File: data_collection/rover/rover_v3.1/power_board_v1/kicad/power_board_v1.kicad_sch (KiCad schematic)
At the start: 127 parts, among them J1 XT60_BATT, J10 from Pi USB2, J11 UPDI prog (UPDI/3V3/GND), J12 XT30 fallback pads, J2 PANEL_SW, J3 USB4105-GF-A (TH shell), J4 USB_A radio1, J5 USB_A radio2, J6 AUX 5V 2A, J7 PI GPIO harness, J8 AUX_CTL out (JST-GH), J9 from Pi USB1, Q2 CSD18543Q3A diode, Q3 CSD18543Q3A switch, U1 LM5145 rail A, U2 LM5145 rail B, U3 ATtiny816 (VQFN), U4 LM74800-Q1, U5 INA226 (addr 0x40), U6 TPS7A1633 3V3 60V LDO, U7 TPS2553 1.7A, U8 TPS2553 1.7A, U9 AP2112K-3.3 (switched)

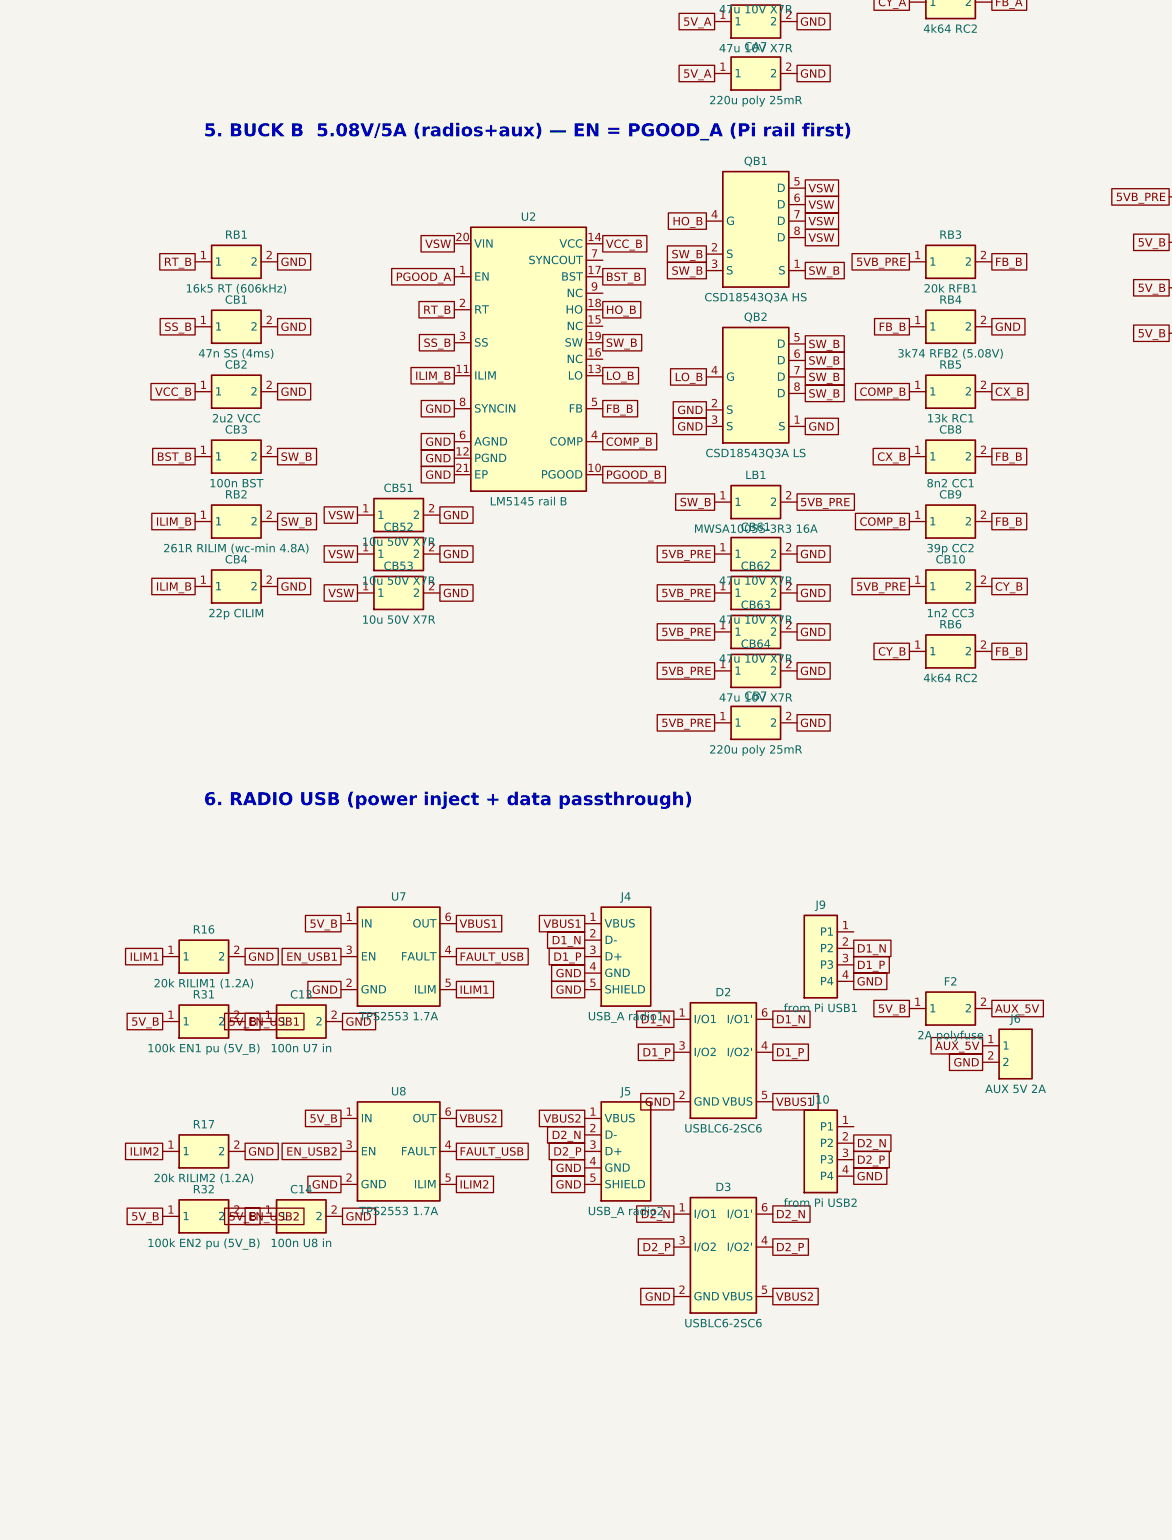
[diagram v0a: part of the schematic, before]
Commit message: USB requirement change: 3rd USB-A port (J13/F3/J14/D8), rail B 5A->6A (RILIM 348), radio-port ILIM to 1.7A max, net classes incl port 3; constraints flagged (TPS2553 1.7A ceiling, non-PD 3A advertisement)
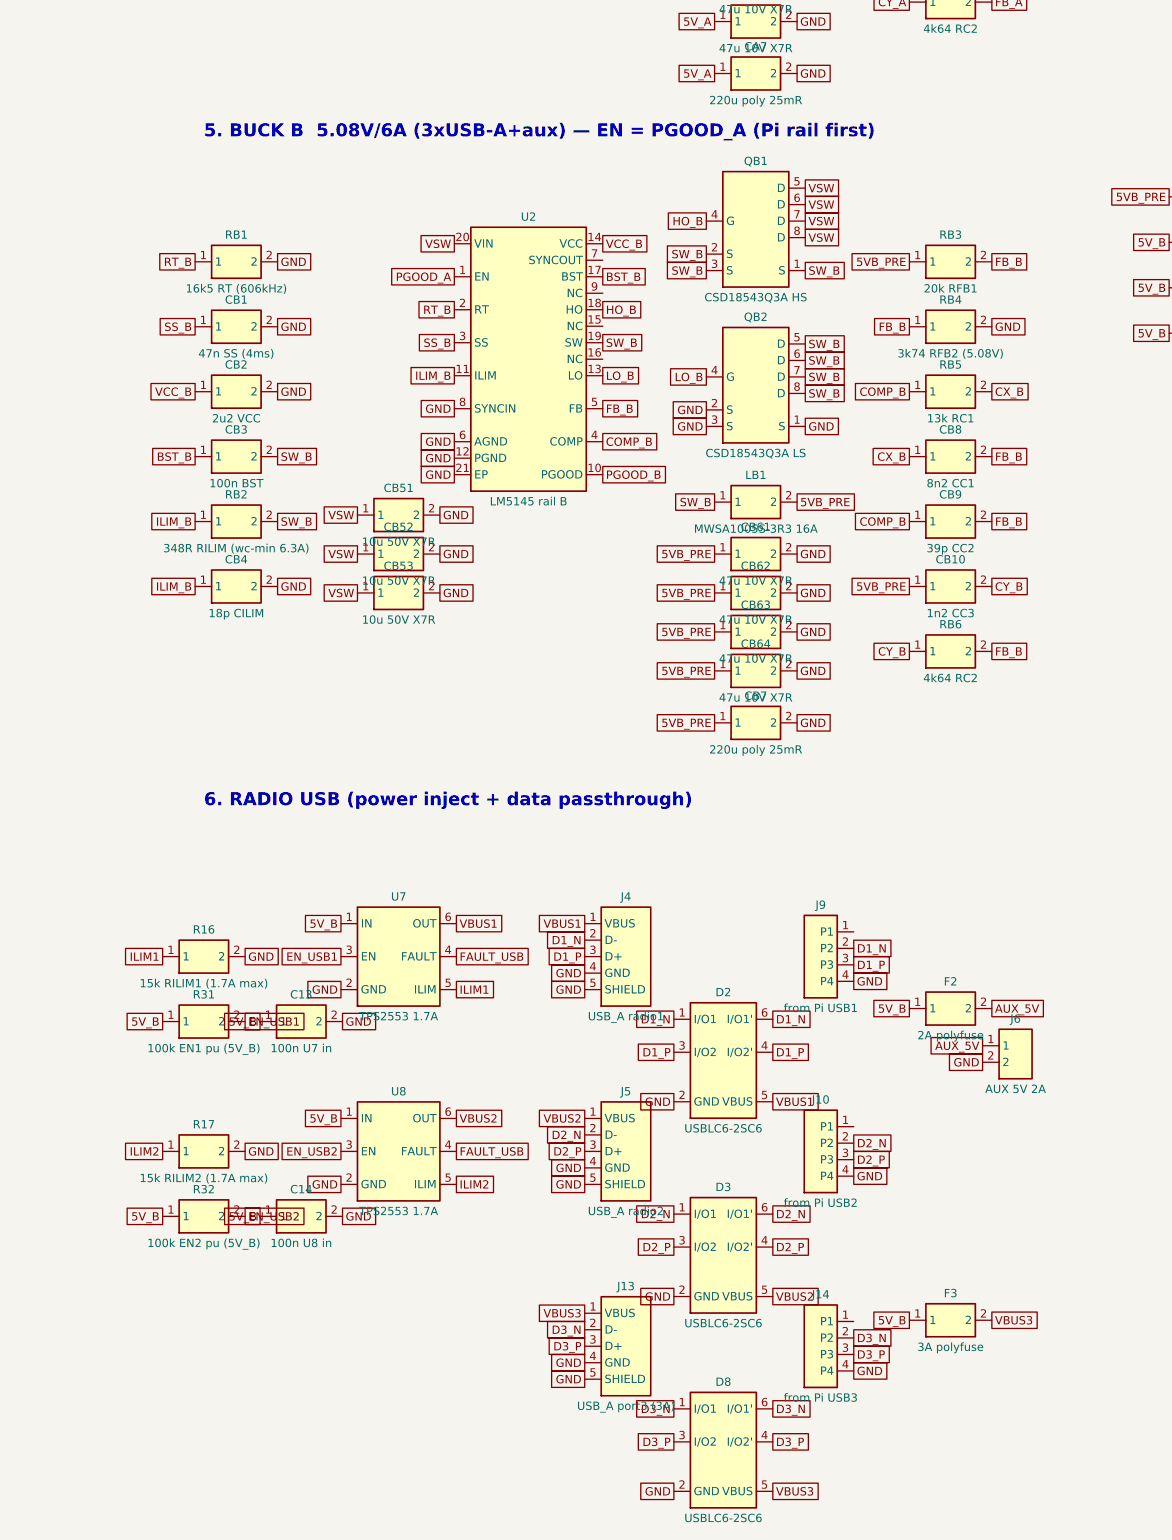
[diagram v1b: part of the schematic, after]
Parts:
- added D8: USBLC6-2SC6, symbol pwr:USBLC6
- added F3: 3A polyfuse, Fuse:FuseHolder_Blade_ATO_Littelfuse_FLR_178.6165, symbol pwr:FUSE
- added J13: USB_A port3 (3A), Connector_USB:USB_A_CNCTech_1001-011-01101_Horizontal, symbol pwr:USB_A
- added J14: from Pi USB3, Connector_PinHeader_2.54mm:PinHeader_1x04_P2.54mm_Vertical, symbol pwr:HDR4
- CB4: value 22p CILIM -> 18p CILIM
- R16: value 20k RILIM1 (1.2A) -> 15k RILIM1 (1.7A max)
- R17: value 20k RILIM2 (1.2A) -> 15k RILIM2 (1.7A max)
- RB2: value 261R RILIM (wc-min 4.8A) -> 348R RILIM (wc-min 6.3A)
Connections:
- net 5V_B: now also F3.1
- net GND: now also D8.2 (GND), J13.4 (GND), J13.5 (SHIELD), J14.4 (P4)
- new net D3_N: D8.1 (I/O1), D8.6 (I/O1'), J13.2 (D-), J14.2 (P2)
- new net D3_P: D8.3 (I/O2), D8.4 (I/O2'), J13.3 (D+), J14.3 (P3)
- new net VBUS3: D8.5 (VBUS), F3.2, J13.1 (VBUS)
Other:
- note added: "5. BUCK B 5.08V/6A (3xUSB-A+aux) — EN = PGOOD_A (Pi rail first)"
- note removed: "5. BUCK B 5.08V/5A (radios+aux) — EN = PGOOD_A (Pi rail first)"

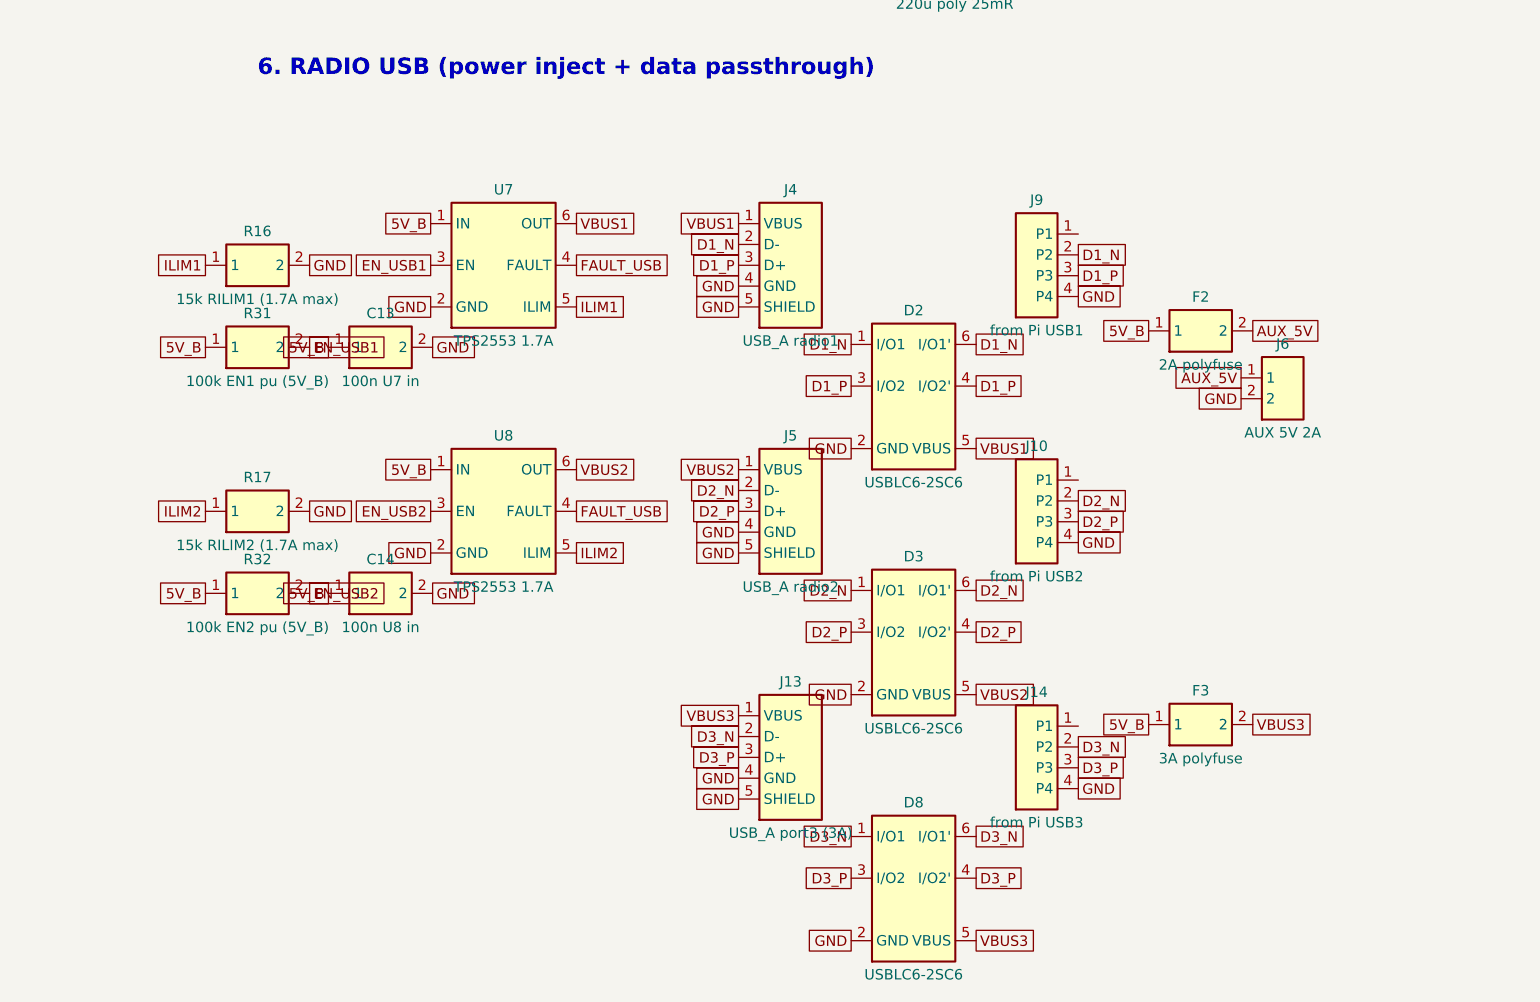
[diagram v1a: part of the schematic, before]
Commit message: All 3 USB-A ports -> TPS2557 (~3A, datasheet-verified DRB pinout SLVS931B): ports 1-2 keep MCU soft-cycling, port 3 always-on; RILIM 20k; rail B 6A per user decision (Pluto spike headroom)
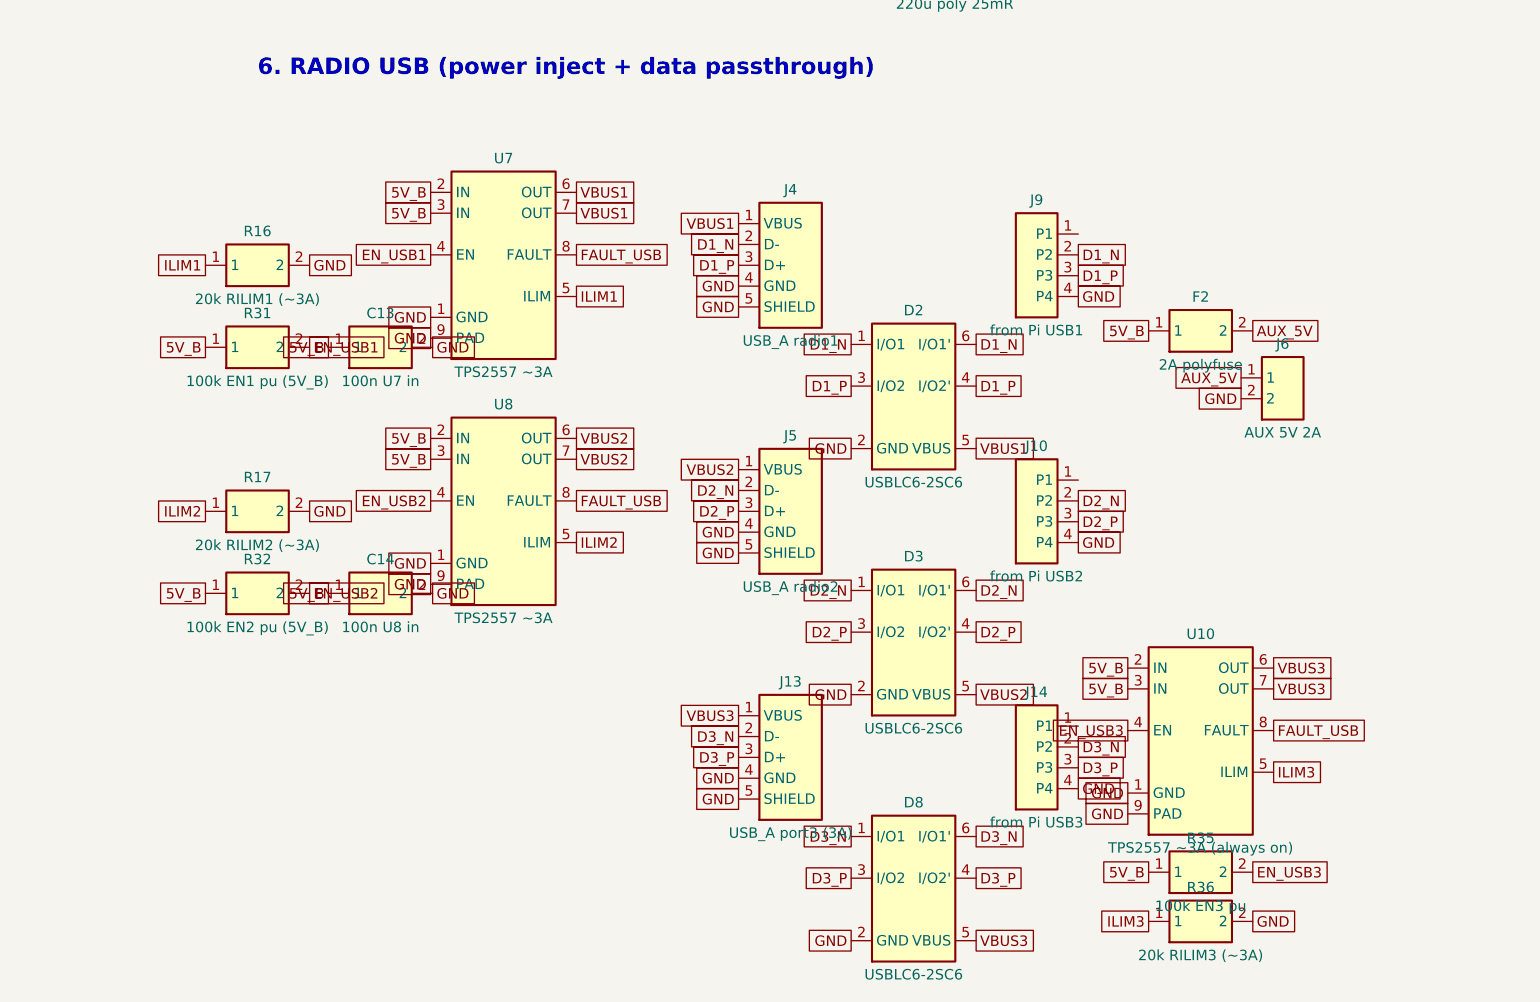
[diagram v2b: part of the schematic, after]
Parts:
- removed F3: 3A polyfuse, Fuse:FuseHolder_Blade_ATO_Littelfuse_FLR_178.6165, symbol pwr:FUSE
- removed U7, U8: TPS2553 1.7A, Package_TO_SOT_SMD:SOT-23-6, symbol pwr:TPS2553
- added R35: 100k EN3 pu, Resistor_SMD:R_0402_1005Metric, symbol pwr:RES
- added R36: 20k RILIM3 (~3A), Resistor_SMD:R_0402_1005Metric, symbol pwr:RES
- added U10: TPS2557 ~3A (always on), Package_SON:VSON-8-1EP_3x3mm_P0.65mm_EP1.65x2.4mm, symbol pwr:TPS2557
- added U7, U8: TPS2557 ~3A, Package_SON:VSON-8-1EP_3x3mm_P0.65mm_EP1.65x2.4mm, symbol pwr:TPS2557
- R16: value 15k RILIM1 (1.7A max) -> 20k RILIM1 (~3A)
- R17: value 15k RILIM2 (1.7A max) -> 20k RILIM2 (~3A)
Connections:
- net 5V_B: now also R35.1, U10.2 (IN), U10.3 (IN), U7.2 (IN), U7.3 (IN), U8.2 (IN), U8.3 (IN)
- net EN_USB1: now also U7.4 (EN)
- net EN_USB2: now also U8.4 (EN)
- net FAULT_USB: now also U10.8 (FAULT), U7.8 (FAULT), U8.8 (FAULT)
- net GND: now also R36.2, U10.1 (GND), U10.9 (PAD), U7.1 (GND), U7.9 (PAD), U8.1 (GND), U8.9 (PAD)
- net ILIM1: now also U7.5 (ILIM)
- net ILIM2: now also U8.5 (ILIM)
- net VBUS1: now also U7.6 (OUT), U7.7 (OUT)
- net VBUS2: now also U8.6 (OUT), U8.7 (OUT)
- net VBUS3: now also U10.6 (OUT), U10.7 (OUT)
- new net EN_USB3: R35.2, U10.4 (EN)
- new net ILIM3: R36.1, U10.5 (ILIM)
